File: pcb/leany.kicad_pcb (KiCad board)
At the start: 4 copper layers, 86.5 x 46.5 mm, 79 parts, among them J1 ST7735S, J2 SWD, J3 USB C, J4 2059-302/998-403, Q1 AO3401A, Q2 AO3400A, Q3 AO3401A, Q4 AO3401A, SW1 SW_HIGH, SW2 SW_HIGH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

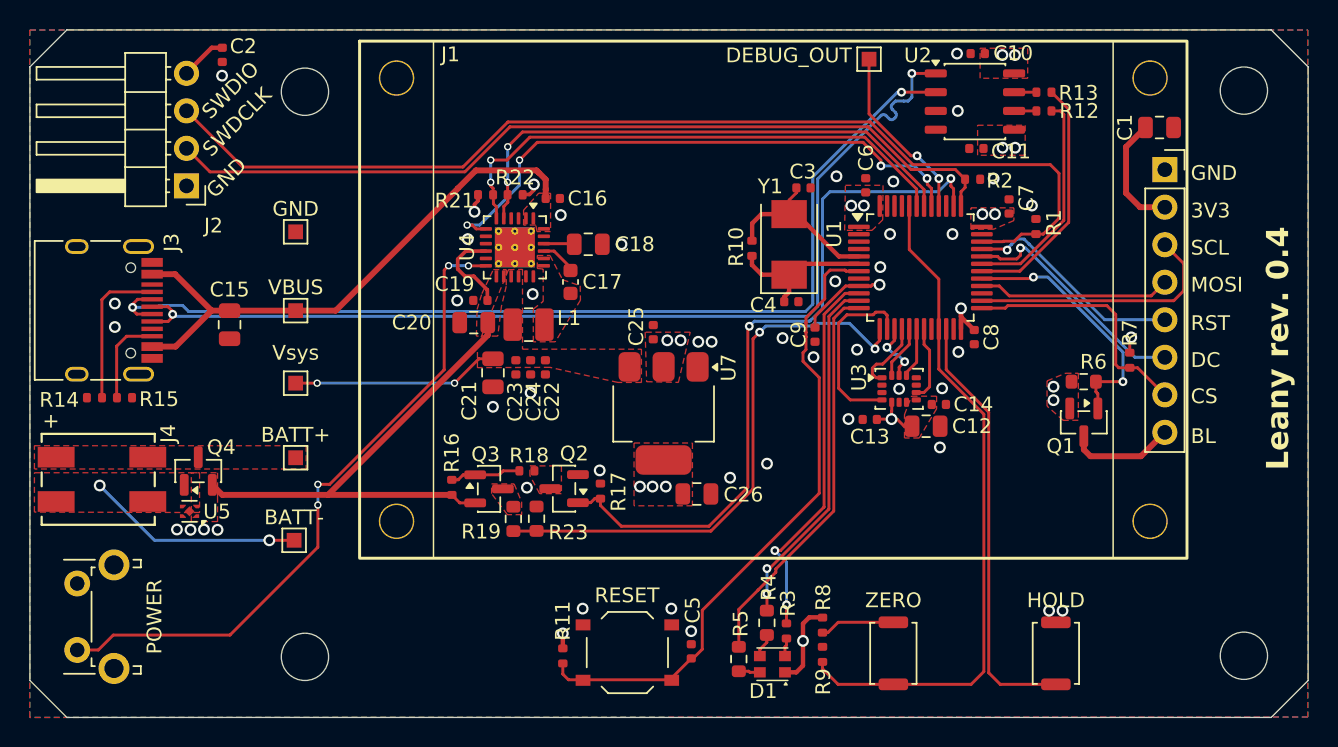
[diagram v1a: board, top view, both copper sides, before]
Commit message: fix: replace the LDO by an AP2112k-3.3 (#93)
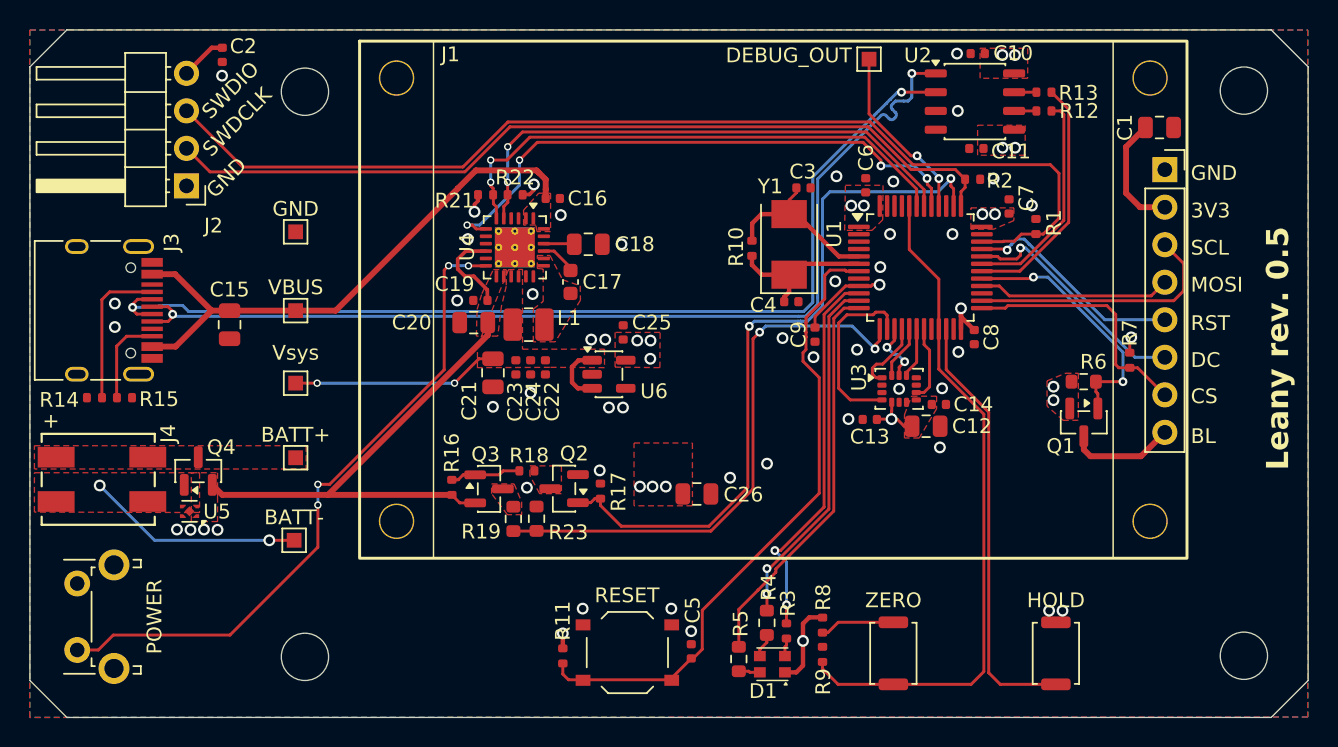
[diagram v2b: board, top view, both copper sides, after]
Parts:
- removed U7: AMS1117-3.3, Package_TO_SOT_SMD:SOT-223-3_TabPin2
- added U6: AP2112K-3.3, Package_TO_SOT_SMD:SOT-23-5, F.Cu at (128.8, 108.5)
- moved C25 2.03 mm to (129.7, 105.7)
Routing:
- net Net-(U6-EN): track 14.1 -> 18.2 mm
- net GND: vias 43 -> 45
- net +3V3: vias 23 -> 24

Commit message: feat: reroute components (#93)
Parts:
- moved C26 8.98 mm to (133.5, 107.8)
- moved C25 3.57 mm to (133.2, 106.2), turned to 0 degrees
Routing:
- net BATT_EN: track 48.7 -> 41.9 mm
- net BATT_VOLT: track 38.3 -> 33.4 mm
- net Net-(U6-EN): track 18.2 -> 17.4 mm
- net USB_D+: track 69.1 -> 69.6 mm
- net USB_D-: track 69.0 -> 69.5 mm
- net GND: vias 45 -> 47
- net +3V3: vias 24 -> 21
